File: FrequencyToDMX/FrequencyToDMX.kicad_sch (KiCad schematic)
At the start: 29 parts, among them J1 DIN-3, J2 AudioJack3_Ground, J3 Conn_01x03_Socket, J4 Conn_01x03, J5 Conn_01x02, J6 Conn_01x05, J7 USB_B, SW1 SW_Push, U1 ATmega168A-P, U2 MAX481E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

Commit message: Modified the schematic and added some code.
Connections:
- net Strobe: no longer RV2.2, U1.26 (PC3)
- net Brightness renamed Brightness_In
- new net Strobe_In: RV2.2, U1.26 (PC3)
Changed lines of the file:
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@@
     (effects (font (size 1.27 1.27)) (justify left bottom))
   )
-  (label "Strobe" (at 53.34 86.36 0) (fields_autoplaced)
+  (label "Strobe_In" (at 53.34 86.36 0) (fields_autoplaced)
     (effects (font (size 1.27 1.27)) (justify left bottom))
   )
@@
     (effects (font (size 1.27 1.27)) (justify left bottom))
   )
-  (label "Brightness" (at 53.34 83.82 0) (fields_autoplaced)
+  (label "Brightness_In" (at 53.34 83.82 0) (fields_autoplaced)
     (effects (font (size 1.27 1.27)) (justify left bottom))
   )

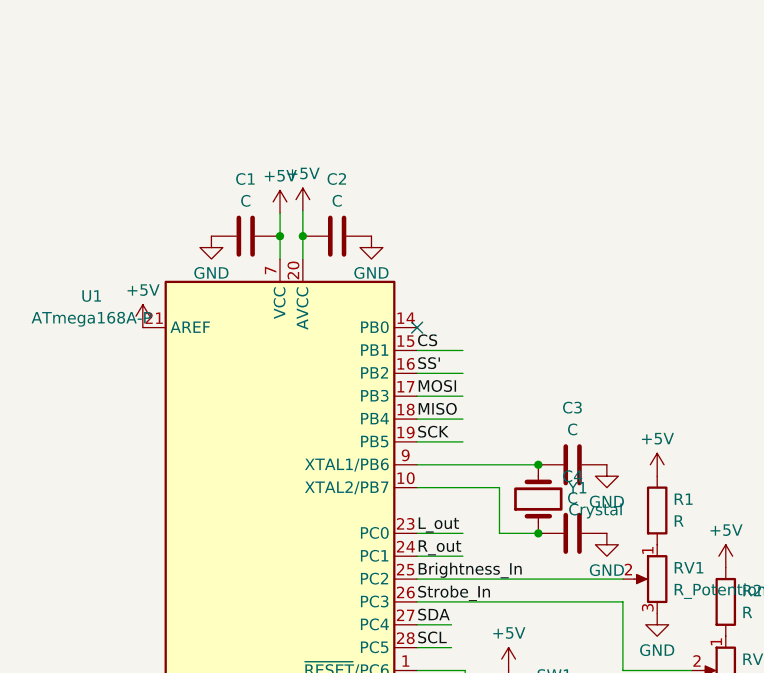
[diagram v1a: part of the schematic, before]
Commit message: Moved utils to own file and added bypass cap in VRef in schematic
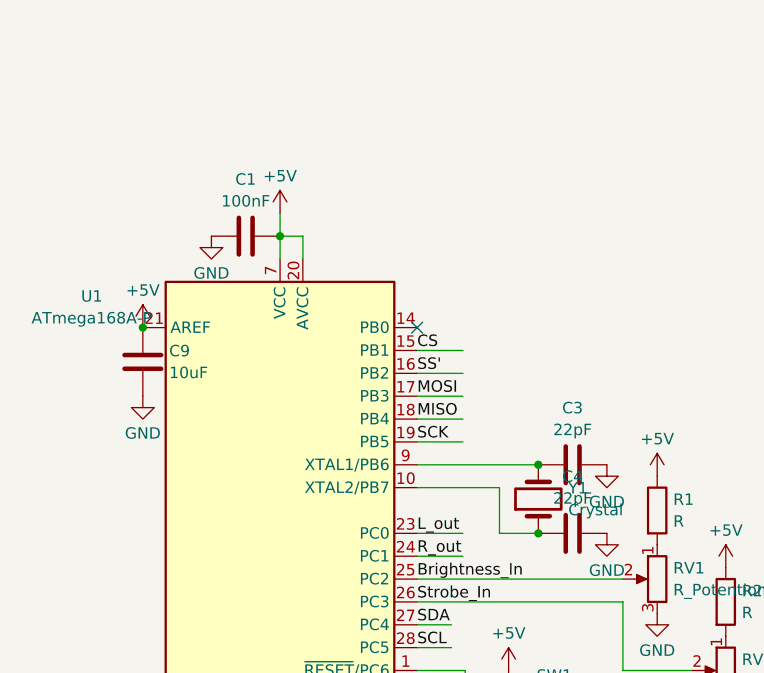
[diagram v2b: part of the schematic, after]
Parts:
- removed C2: C, symbol Device:C
- added C9: 10uF, symbol Device:C
- C1: value C -> 100nF
- C3, C4: value C -> 22pF
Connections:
- net +5V: now also C9.1
- net GND: now also C9.2
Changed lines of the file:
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@@
 (kicad_sch (version 20230121) (generator eeschema)
   (paper "A4")
-  (junction (at 40.64 45.72) (diameter 0) (color 0 0 0 0)
-  )
   (junction (at 63.5 101.6) (diameter 0) (color 0 0 0 0)
   )
@@
   (junction (at 66.802 78.74) (diameter 0) (color 0 0 0 0)
   )
+  (junction (at 22.86 55.88) (diameter 0) (color 0 0 0 0)
+  )
   (junction (at 261.874 76.2) (diameter 0) (color 0 0 0 0)
   )
@@
   (junction (at 134.62 25.4) (diameter 0) (color 0 0 0 0)
   )
+  (junction (at 30.48 170.18) (diameter 0) (color 0 0 0 0)
+  )
   (junction (at 38.1 45.72) (diameter 0) (color 0 0 0 0)
-  )
-  (junction (at 30.48 170.18) (diameter 0) (color 0 0 0 0)
   )
   (no_connect (at 53.34 104.14))
@@
     (stroke (width 0) (type default))
   )
+  (wire (pts (xy 38.1 45.72) (xy 40.64 45.72))
+    (stroke (width 0) (type default))
+  )
   (wire (pts (xy 53.34 101.6) (xy 57.404 101.6))
     (stroke (width 0) (type default))
@@
     (stroke (width 0) (type default))
   )
+  (wire (pts (xy 38.1 45.72) (xy 38.1 48.26))
+    (stroke (width 0) (type default))
+  )
   (wire (pts (xy 223.52 30.48) (xy 231.14 30.48))
     (stroke (width 0) (type default))
@@
     (stroke (width 0) (type default))
   )
+  (wire (pts (xy 53.34 86.36) (xy 76.2 86.36))
+    (stroke (width 0) (type default))
+  )
+  (wire (pts (xy 226.06 71.12) (xy 231.14 71.12))
+    (stroke (width 0) (type default))
+  )
+  (wire (pts (xy 208.28 69.342) (xy 212.09 69.342))
+    (stroke (width 0) (type default))
+  )
+  (wire (pts (xy 53.34 68.58) (xy 58.42 68.58))
+    (stroke (width 0) (type default))
+  )
+  (wire (pts (xy 53.34 71.12) (xy 66.802 71.12))
+    (stroke (width 0) (type default))
+  )
+  (wire (pts (xy 53.34 60.96) (xy 58.42 60.96))
+    (stroke (width 0) (type default))
+  )
+  (wire (pts (xy 144.78 43.18) (xy 152.4 43.18))
+    (stroke (width 0) (type default))
+  )
+  (wire (pts (xy 53.34 81.28) (xy 58.42 81.28))
+    (stroke (width 0) (type default))
+  )
   (wire (pts (xy 38.1 43.18) (xy 38.1 45.72))
     (stroke (width 0) (type default))
   )
-  (wire (pts (xy 53.34 86.36) (xy 76.2 86.36))
-    (stroke (width 0) (type default))
-  )
-  (wire (pts (xy 226.06 71.12) (xy 231.14 71.12))
-    (stroke (width 0) (type default))
-  )
-  (wire (pts (xy 208.28 69.342) (xy 212.09 69.342))
-    (stroke (width 0) (type default))
-  )
-  (wire (pts (xy 53.34 68.58) (xy 58.42 68.58))
-    (stroke (width 0) (type default))
-  )
-  (wire (pts (xy 53.34 71.12) (xy 66.802 71.12))
-    (stroke (width 0) (type default))
-  )
-  (wire (pts (xy 53.34 60.96) (xy 58.42 60.96))
-    (stroke (width 0) (type default))
-  )
-  (wire (pts (xy 144.78 43.18) (xy 152.4 43.18))
-    (stroke (width 0) (type default))
-  )
-  (wire (pts (xy 53.34 81.28) (xy 58.42 81.28))
-    (stroke (width 0) (type default))
-  )
-  (wire (pts (xy 38.1 45.72) (xy 38.1 48.26))
-    (stroke (width 0) (type default))
-  )
   (wire (pts (xy 223.52 60.96) (xy 231.14 60.96))
     (stroke (width 0) (type default))
@@
     (stroke (width 0) (type default))
   )
+  (wire (pts (xy 40.64 45.72) (xy 40.64 48.26))
+    (stroke (width 0) (type default))
+  )
   (wire (pts (xy 256.54 43.18) (xy 261.874 43.18))
     (stroke (width 0) (type default))
@@
     (stroke (width 0) (type default))
   )
-  (wire (pts (xy 40.64 42.926) (xy 40.64 45.72))
-    (stroke (width 0) (type default))
-  )
   (wire (pts (xy 53.34 83.82) (xy 76.2 83.82))
     (stroke (width 0) (type default))
@@
     (stroke (width 0) (type default))
   )
-  (wire (pts (xy 40.64 45.72) (xy 40.64 48.26))
-    (stroke (width 0) (type default))
-  )
   (wire (pts (xy 76.2 86.36) (xy 76.2 93.98))
     (stroke (width 0) (type default))
@@
         (path "/56c3bbfa-7886-4f28-8999-0145aad421e7"
           (reference "#PWR05") (unit 1)
+        )
+      )
+    )
+  )
+  (symbol (lib_id "Device:C") (at 22.86 59.69 0) (unit 1)
+    (in_bom yes) (on_board yes) (dnp no) (fields_autoplaced)
+    (property "Reference" "C9" (at 25.781 58.4779 0)
+      (effects (font (size 1.27 1.27)) (justify left))
+    )
+    (property "Value" "10uF" (at 25.781 60.9021 0)
+      (effects (font (size 1.27 1.27)) (justify left))
+    )
+    (property "Footprint" "" (at 23.8252 63.5 0)
+      (effects (font (size 1.27 1.27)) hide)
+    )
+    (property "Datasheet" "~" (at 22.86 59.69 0)
+      (effects (font (size 1.27 1.27)) hide)
+    )
+    (pin "1")
+    (pin "2")
+    (instances
+      (project "FrequencyToDMX"
+        (path "/56c3bbfa-7886-4f28-8999-0145aad421e7"
+          (reference "C9") (unit 1)
         )
       )
@@
       (effects (font (size 1.27 1.27)))
     )
-    (property "Value" "C" (at 34.29 41.8409 90)
+    (property "Value" "100nF" (at 34.29 41.8409 90)
       (effects (font (size 1.27 1.27)))
     )
@@
     )
   )
-  (symbol (lib_id "Device:C") (at 44.45 45.72 90) (unit 1)
-    (in_bom yes) (on_board yes) (dnp no) (fields_autoplaced)
-    (property "Reference" "C2" (at 44.45 39.4167 90)
-      (effects (font (size 1.27 1.27)))
-    )
-    (property "Value" "C" (at 44.45 41.8409 90)
-      (effects (font (size 1.27 1.27)))
-    )
-    (property "Footprint" "" (at 48.26 44.7548 0)
-      (effects (font (size 1.27 1.27)) hide)
-    )
-    (property "Datasheet" "~" (at 44.45 45.72 0)
-      (effects (font (size 1.27 1.27)) hide)
-    )
-    (pin "1")
-    (pin "2")
-    (instances
-      (project "FrequencyToDMX"
-        (path "/56c3bbfa-7886-4f28-8999-0145aad421e7"
-          (reference "C2") (unit 1)
-        )
-      )
-    )
-  )
   (symbol (lib_id "power:+5V") (at 124.46 40.64 90) (unit 1)
     (in_bom yes) (on_board yes) (dnp no) (fields_autoplaced)
@@
     )
   )
-  (symbol (lib_id "power:GND") (at 48.26 45.72 0) (unit 1)
-    (in_bom yes) (on_board yes) (dnp no) (fields_autoplaced)
-    (property "Reference" "#PWR010" (at 48.26 52.07 0)
-      (effects (font (size 1.27 1.27)) hide)
-    )
-    (property "Value" "GND" (at 48.26 49.8531 0)
-      (effects (font (size 1.27 1.27)))
-    )
-    (property "Footprint" "" (at 48.26 45.72 0)
-      (effects (font (size 1.27 1.27)) hide)
-    )
-    (property "Datasheet" "" (at 48.26 45.72 0)
-      (effects (font (size 1.27 1.27)) hide)
-    )
-    (pin "1")
-    (instances
-      (project "FrequencyToDMX"
-        (path "/56c3bbfa-7886-4f28-8999-0145aad421e7"
-          (reference "#PWR010") (unit 1)
-        )
-      )
-    )
-  )
   (symbol (lib_id "Device:C") (at 231.14 80.01 0) (unit 1)
     (in_bom yes) (on_board yes) (dnp no) (fields_autoplaced)
@@
       (effects (font (size 1.27 1.27)))
     )
-    (property "Value" "C" (at 70.612 74.8609 90)
+    (property "Value" "22pF" (at 70.612 74.8609 90)
       (effects (font (size 1.27 1.27)))
     )
@@
     )
   )
-  (symbol (lib_id "power:+5V") (at 40.64 42.926 0) (unit 1)
-    (in_bom yes) (on_board yes) (dnp no) (fields_autoplaced)
-    (property "Reference" "#PWR08" (at 40.64 46.736 0)
-      (effects (font (size 1.27 1.27)) hide)
-    )
-    (property "Value" "+5V" (at 40.64 38.7929 0)
-      (effects (font (size 1.27 1.27)))
-    )
-    (property "Footprint" "" (at 40.64 42.926 0)
-      (effects (font (size 1.27 1.27)) hide)
-    )
-    (property "Datasheet" "" (at 40.64 42.926 0)
-      (effects (font (size 1.27 1.27)) hide)
-    )
-    (pin "1")
-    (instances
-      (project "FrequencyToDMX"
-        (path "/56c3bbfa-7886-4f28-8999-0145aad421e7"
-          (reference "#PWR08") (unit 1)
-        )
-      )
-    )
-  )
   (symbol (lib_id "power:+5V") (at 243.84 22.86 0) (mirror y) (unit 1)
     (in_bom yes) (on_board yes) (dnp no) (fields_autoplaced)
@@
         (path "/56c3bbfa-7886-4f28-8999-0145aad421e7"
           (reference "#PWR01") (unit 1)
+        )
+      )
+    )
+  )
+  (symbol (lib_id "power:GND") (at 22.86 63.5 0) (unit 1)
+    (in_bom yes) (on_board yes) (dnp no) (fields_autoplaced)
+    (property "Reference" "#PWR036" (at 22.86 69.85 0)
+      (effects (font (size 1.27 1.27)) hide)
+    )
+    (property "Value" "GND" (at 22.86 67.6331 0)
+      (effects (font (size 1.27 1.27)))
+    )
+    (property "Footprint" "" (at 22.86 63.5 0)
+      (effects (font (size 1.27 1.27)) hide)
+    )
+    (property "Datasheet" "" (at 22.86 63.5 0)
+      (effects (font (size 1.27 1.27)) hide)
+    )
+    (pin "1")
+    (instances
+      (project "FrequencyToDMX"
+        (path "/56c3bbfa-7886-4f28-8999-0145aad421e7"
+          (reference "#PWR036") (unit 1)
         )
       )
@@
       (effects (font (size 1.27 1.27)))
     )
-    (property "Value" "C" (at 70.612 67.2409 90)
-      (effects (font (size 1.27 1.27)))
-    )
+    (property "Value" "22pF" (at 70.612 67.2409 90)
+      (effects (font (size 1.27 1.27)))
+    )
